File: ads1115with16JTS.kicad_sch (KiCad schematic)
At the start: 50 parts, among them J1 Conn_01x02_Pin, J10 Conn_01x02_Pin, J11 Conn_01x02_Pin, J12 Conn_01x02_Pin, J13 Conn_01x02_Pin, J14 Conn_01x02_Pin, J15 Conn_01x02_Pin, J16 Conn_01x02_Pin, J17 Conn_01x04_Pin, J18 PinSocket_1x20_P2.54mm_Vertic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, J19 PinSocket_1x20_P2.54mm_Vertic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, J2 Conn_01x02_Pin, J20 Screw_Terminal_01x02, J3 Conn_01x02_Pin, J4 Conn_01x02_Pin, J5 Conn_01x02_Pin, J6 Conn_01x02_Pin, J7 Conn_01x02_Pin, J8 Conn_01x02_Pin, J9 Conn_01x02_Pin, U1 ADS1115IDGS, U2 ADS1115IDGS, U3 ADS1115IDGS, U4 ADS1115IDGS

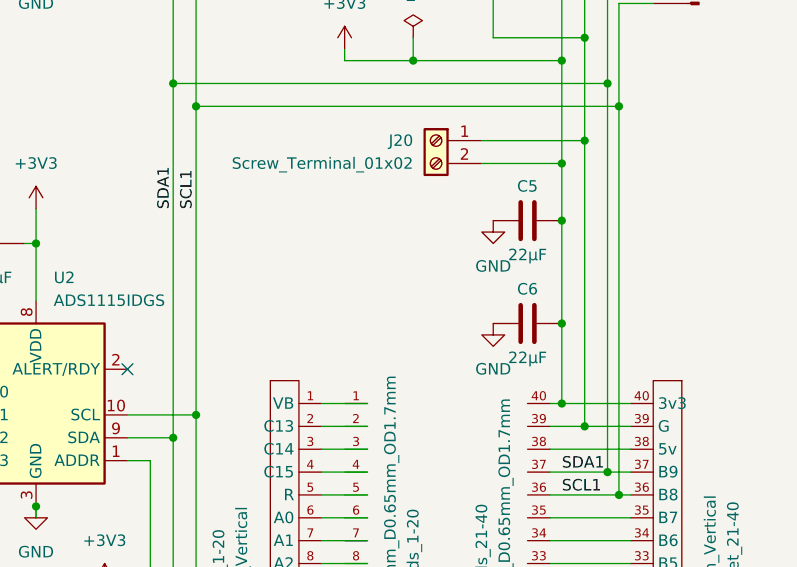
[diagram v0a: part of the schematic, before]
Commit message: added 2 more noise caps on power line. Ongoing attempt to update PCB from schematic and keep footprint links to ProjectLib.
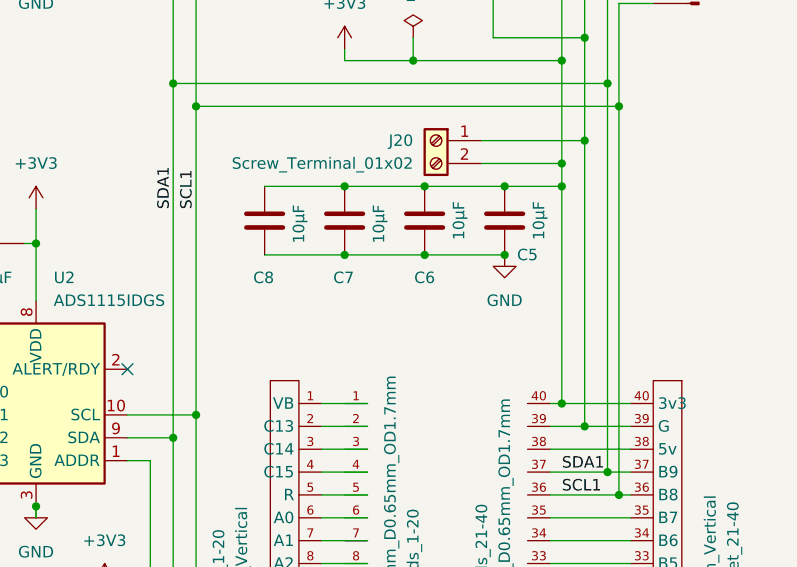
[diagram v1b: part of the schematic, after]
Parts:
- added C7, C8: 10µF, ProjectLib:C_0805_2012Metric, symbol Device:C
- C5, C6: value 22µF -> 10µF
- J17: footprint Connector_JST:JST_XH_B4B-XH-A_1x04_P2.50mm_Vertical -> ProjectLib:JST_XH_B4B-XH-A_1x04_P2.50mm_Vertical
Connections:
- net +3V3: now also C7.1, C8.1
- net GND: now also C7.2, C8.2
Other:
- moved on the sheet: C5, C6
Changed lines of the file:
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@@
   (junction (at 50.8 100.33) (diameter 0) (color 0 0 0 0)
   )
+  (junction (at 168.91 86.36) (diameter 0) (color 0 0 0 0)
+  )
   (junction (at 143.51 215.9) (diameter 0) (color 0 0 0 0)
   )
+  (junction (at 160.02 86.36) (diameter 0) (color 0 0 0 0)
+  )
   (junction (at 49.53 127) (diameter 0) (color 0 0 0 0)
   )
@@
   (junction (at 48.26 66.04) (diameter 0) (color 0 0 0 0)
   )
+  (junction (at 177.8 86.36) (diameter 0) (color 0 0 0 0)
+  )
   (junction (at 140.97 67.31) (diameter 0) (color 0 0 0 0)
   )
@@
   (junction (at 125.73 142.24) (diameter 0) (color 0 0 0 0)
   )
+  (junction (at 177.8 78.74) (diameter 0) (color 0 0 0 0)
+  )
   (junction (at 143.51 104.14) (diameter 0) (color 0 0 0 0)
   )
@@
   (junction (at 143.51 69.85) (diameter 0) (color 0 0 0 0)
   )
-  (junction (at 184.15 93.98) (diameter 0) (color 0 0 0 0)
-  )
   (junction (at 184.15 76.2) (diameter 0) (color 0 0 0 0)
   )
+  (junction (at 168.91 78.74) (diameter 0) (color 0 0 0 0)
+  )
   (junction (at 190.5 113.03) (diameter 0) (color 0 0 0 0)
   )
@@
   (junction (at 167.64 64.77) (diameter 0) (color 0 0 0 0)
   )
+  (junction (at 160.02 78.74) (diameter 0) (color 0 0 0 0)
+  )
   (junction (at 48.26 184.15) (diameter 0) (color 0 0 0 0)
   )
@@
   (junction (at 189.23 110.49) (diameter 0) (color 0 0 0 0)
   )
+  (junction (at 184.15 78.74) (diameter 0) (color 0 0 0 0)
+  )
   (junction (at 49.53 250.19) (diameter 0) (color 0 0 0 0)
   )
@@
   )
   (junction (at 48.26 157.48) (diameter 0) (color 0 0 0 0)
-  )
-  (junction (at 184.15 82.55) (diameter 0) (color 0 0 0 0)
   )
   (junction (at 48.26 39.37) (diameter 0) (color 0 0 0 0)
@@
     (stroke (width 0) (type default))
   )
+  (wire (pts (xy 177.8 78.74) (xy 184.15 78.74))
+    (stroke (width 0) (type default))
+  )
   (wire (pts (xy 88.9 227.33) (xy 88.9 218.44))
     (stroke (width 0) (type default))
@@
     (stroke (width 0) (type default))
   )
-  (wire (pts (xy 184.15 76.2) (xy 184.15 82.55))
+  (wire (pts (xy 184.15 76.2) (xy 184.15 78.74))
     (stroke (width 0) (type default))
   )
@@
     (stroke (width 0) (type default))
   )
+  (wire (pts (xy 151.13 86.36) (xy 160.02 86.36))
+    (stroke (width 0) (type default))
+  )
   (wire (pts (xy 143.51 215.9) (xy 143.51 220.98))
     (stroke (width 0) (type default))
@@
     (stroke (width 0) (type default))
   )
+  (wire (pts (xy 151.13 78.74) (xy 160.02 78.74))
+    (stroke (width 0) (type default))
+  )
   (wire (pts (xy 182.88 123.19) (xy 191.77 123.19))
     (stroke (width 0) (type default))
@@
     (stroke (width 0) (type default))
   )
-  (wire (pts (xy 184.15 93.98) (xy 184.15 102.87))
-    (stroke (width 0) (type default))
-  )
   (wire (pts (xy 125.73 85.09) (xy 125.73 91.44))
     (stroke (width 0) (type default))
@@
     (stroke (width 0) (type default))
   )
-  (wire (pts (xy 184.15 82.55) (xy 184.15 93.98))
-    (stroke (width 0) (type default))
-  )
   (wire (pts (xy 157.48 105.41) (xy 162.56 105.41))
     (stroke (width 0) (type default))
@@
     (stroke (width 0) (type default))
   )
+  (wire (pts (xy 184.15 78.74) (xy 184.15 102.87))
+    (stroke (width 0) (type default))
+  )
   (wire (pts (xy 157.48 120.65) (xy 162.56 120.65))
     (stroke (width 0) (type default))
@@
     (stroke (width 0) (type default))
   )
+  (wire (pts (xy 160.02 78.74) (xy 168.91 78.74))
+    (stroke (width 0) (type default))
+  )
+  (wire (pts (xy 168.91 86.36) (xy 177.8 86.36))
+    (stroke (width 0) (type default))
+  )
+  (wire (pts (xy 160.02 86.36) (xy 168.91 86.36))
+    (stroke (width 0) (type default))
+  )
   (wire (pts (xy 118.11 227.33) (xy 118.11 220.98))
     (stroke (width 0) (type default))
@@
   )
   (wire (pts (xy 189.23 55.88) (xy 189.23 67.31))
+    (stroke (width 0) (type default))
+  )
+  (wire (pts (xy 168.91 78.74) (xy 177.8 78.74))
     (stroke (width 0) (type default))
   )
@@
     )
   )
-  (symbol (lib_id "ProjectLib:C") (at 180.34 93.98 270) (mirror x) (unit 1)
+  (symbol (lib_id "ProjectLib:C") (at 168.91 82.55 0) (mirror y) (unit 1)
     (in_bom yes) (on_board yes) (dnp no)
-    (property "Reference" "C6" (at 180.34 90.17 90)
-      (effects (font (size 1.27 1.27)))
-    )
-    (property "Value" "22µF" (at 180.34 97.79 90)
-      (effects (font (size 1.27 1.27)))
-    )
-    (property "Footprint" "Capacitor_SMD:C_0805_2012Metric" (at 176.53 93.0148 0)
-      (effects (font (size 1.27 1.27)) hide)
-    )
-    (property "Datasheet" "~" (at 180.34 93.98 0)
+    (property "Reference" "C6" (at 168.91 88.9 0)
+      (effects (font (size 1.27 1.27)))
+    )
+    (property "Value" "10µF" (at 172.72 82.55 90)
+      (effects (font (size 1.27 1.27)))
+    )
+    (property "Footprint" "Capacitor_SMD:C_0805_2012Metric" (at 167.9448 86.36 0)
+      (effects (font (size 1.27 1.27)) hide)
+    )
+    (property "Datasheet" "~" (at 168.91 82.55 0)
       (effects (font (size 1.27 1.27)) hide)
     )
@@
     )
   )
+  (symbol (lib_id "Device:C") (at 151.13 82.55 0) (unit 1)
+    (in_bom yes) (on_board yes) (dnp no)
+    (property "Reference" "C8" (at 149.86 88.9 0)
+      (effects (font (size 1.27 1.27)) (justify left))
+    )
+    (property "Value" "10µF" (at 154.94 85.09 90)
+      (effects (font (size 1.27 1.27)) (justify left))
+    )
+    (property "Footprint" "ProjectLib:C_0805_2012Metric" (at 152.0952 86.36 0)
+      (effects (font (size 1.27 1.27)) hide)
+    )
+    (property "Datasheet" "~" (at 151.13 82.55 0)
+      (effects (font (size 1.27 1.27)) hide)
+    )
+    (pin "1")
+    (pin "2")
+    (instances
+      (project "ads1115with16JTS"
+        (path "/0c2d0c14-8850-4a30-bb78-b2f40cb442ba"
+          (reference "C8") (unit 1)
+        )
+      )
+    )
+  )
   (symbol (lib_id "ProjectLib:Conn_01x02_Pin") (at 44.45 127 0) (unit 1)
     (in_bom yes) (on_board yes) (dnp no)
@@
     )
   )
-  (symbol (lib_id "power:GND") (at 176.53 82.55 0) (unit 1)
-    (in_bom yes) (on_board yes) (dnp no) (fields_autoplaced)
-    (property "Reference" "#PWR050" (at 176.53 88.9 0)
-      (effects (font (size 1.27 1.27)) hide)
-    )
-    (property "Value" "GND" (at 176.53 87.63 0)
-      (effects (font (size 1.27 1.27)))
-    )
-    (property "Footprint" "" (at 176.53 82.55 0)
-      (effects (font (size 1.27 1.27)) hide)
-    )
-    (property "Datasheet" "" (at 176.53 82.55 0)
+  (symbol (lib_id "power:GND") (at 177.8 86.36 0) (unit 1)
+    (in_bom yes) (on_board yes) (dnp no) (fields_autoplaced)
+    (property "Reference" "#PWR050" (at 177.8 92.71 0)
+      (effects (font (size 1.27 1.27)) hide)
+    )
+    (property "Value" "GND" (at 177.8 91.44 0)
+      (effects (font (size 1.27 1.27)))
+    )
+    (property "Footprint" "" (at 177.8 86.36 0)
+      (effects (font (size 1.27 1.27)) hide)
+    )
+    (property "Datasheet" "" (at 177.8 86.36 0)
       (effects (font (size 1.27 1.27)) hide)
     )
@@
     )
   )
-  (symbol (lib_id "ProjectLib:C") (at 180.34 82.55 270) (mirror x) (unit 1)
+  (symbol (lib_id "ProjectLib:C") (at 177.8 82.55 0) (mirror y) (unit 1)
     (in_bom yes) (on_board yes) (dnp no)
-    (property "Reference" "C5" (at 180.34 78.74 90)
-      (effects (font (size 1.27 1.27)))
-    )
-    (property "Value" "22µF" (at 180.34 86.36 90)
-      (effects (font (size 1.27 1.27)))
-    )
-    (property "Footprint" "Capacitor_SMD:C_0805_2012Metric" (at 176.53 81.5848 0)
-      (effects (font (size 1.27 1.27)) hide)
-    )
-    (property "Datasheet" "~" (at 180.34 82.55 0)
+    (property "Reference" "C5" (at 180.34 86.36 0)
+      (effects (font (size 1.27 1.27)))
+    )
+    (property "Value" "10µF" (at 181.61 82.55 90)
+      (effects (font (size 1.27 1.27)))
+    )
+    (property "Footprint" "Capacitor_SMD:C_0805_2012Metric" (at 176.8348 86.36 0)
+      (effects (font (size 1.27 1.27)) hide)
+    )
+    (property "Datasheet" "~" (at 177.8 82.55 0)
       (effects (font (size 1.27 1.27)) hide)
     )
@@
         (path "/0c2d0c14-8850-4a30-bb78-b2f40cb442ba"
           (reference "#PWR02") (unit 1)
-        )
-      )
-    )
-  )
-  (symbol (lib_id "power:GND") (at 176.53 93.98 0) (unit 1)
-    (in_bom yes) (on_board yes) (dnp no) (fields_autoplaced)
-    (property "Reference" "#PWR051" (at 176.53 100.33 0)
-      (effects (font (size 1.27 1.27)) hide)
-    )
-    (property "Value" "GND" (at 176.53 99.06 0)
-      (effects (font (size 1.27 1.27)))
-    )
-    (property "Footprint" "" (at 176.53 93.98 0)
-      (effects (font (size 1.27 1.27)) hide)
-    )
-    (property "Datasheet" "" (at 176.53 93.98 0)
-      (effects (font (size 1.27 1.27)) hide)
-    )
-    (pin "1")
-    (instances
-      (project "ads1115with16JTS"
-        (path "/0c2d0c14-8850-4a30-bb78-b2f40cb442ba"
-          (reference "#PWR051") (unit 1)
         )
       )
@@
       (effects (font (size 1.27 1.27)))
     )
-    (property "Footprint" "Connector_JST:JST_XH_B4B-XH-A_1x04_P2.50mm_Vertical" (at 199.39 53.34 0)
+    (property "Footprint" "ProjectLib:JST_XH_B4B-XH-A_1x04_P2.50mm_Vertical" (at 199.39 53.34 0)
       (effects (font (size 1.27 1.27)) hide)
     )
@@
         )
       )
+    )
+  )
+  (symbol (lib_id "Device:C") (at 160.02 82.55 0) (unit 1)
+    (in_bom yes) (on_board yes) (dnp no)
+    (property "Reference" "C7" (at 158.75 88.9 0)
+      (effects (font (size 1.27 1.27)) (justify left))
+    )
+    (property "Value" "10µF" (at 163.83 85.09 90)
+      (effects (font (size 1.27 1.27)) (justify left))
+    )
+    (property "Footprint" "ProjectLib:C_0805_2012Metric" (at 160.9852 86.36 0)
+      (effects (font (size 1.27 1.27)) hide)
+    )
+    (property "Datasheet" "~" (at 160.02 82.55 0)
+      (effects (font (size 1.27 1.27)) hide)
+    )
+    (pin "1")
+    (pin "2")
+    (instances
+      (project "ads1115with16JTS"
+        (path "/0c2d0c14-8850-4a30-bb78-b2f40cb442ba"
+          (reference "C7") (unit 1)
+        )
+      )

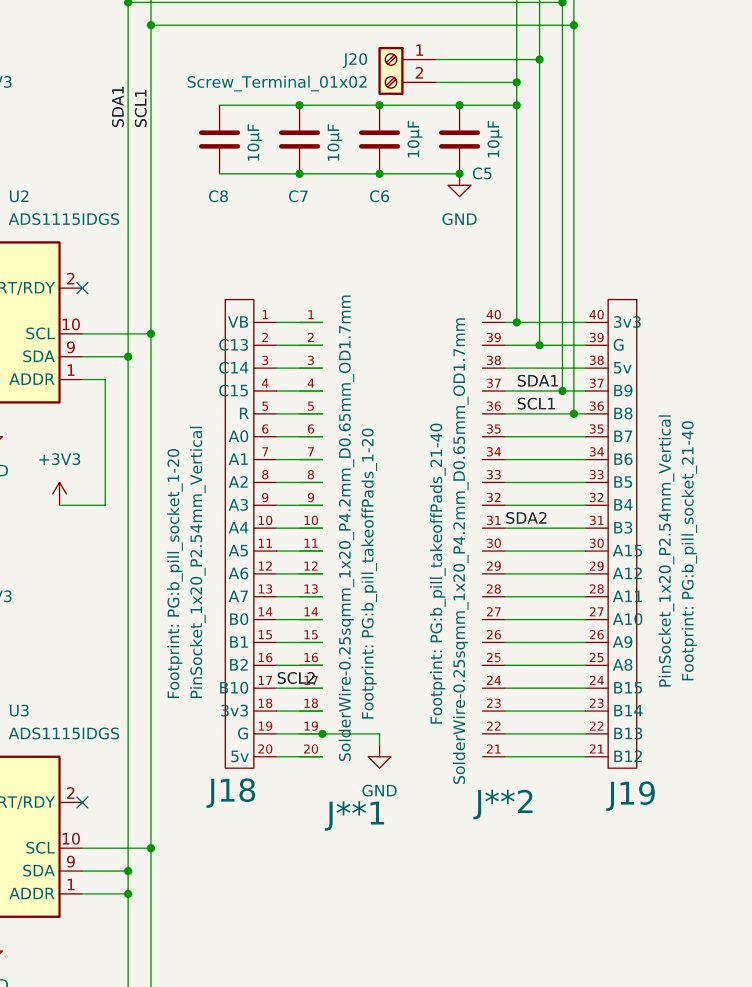
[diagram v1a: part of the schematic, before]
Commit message: added 2 more power noise caps and changed to 10muF.
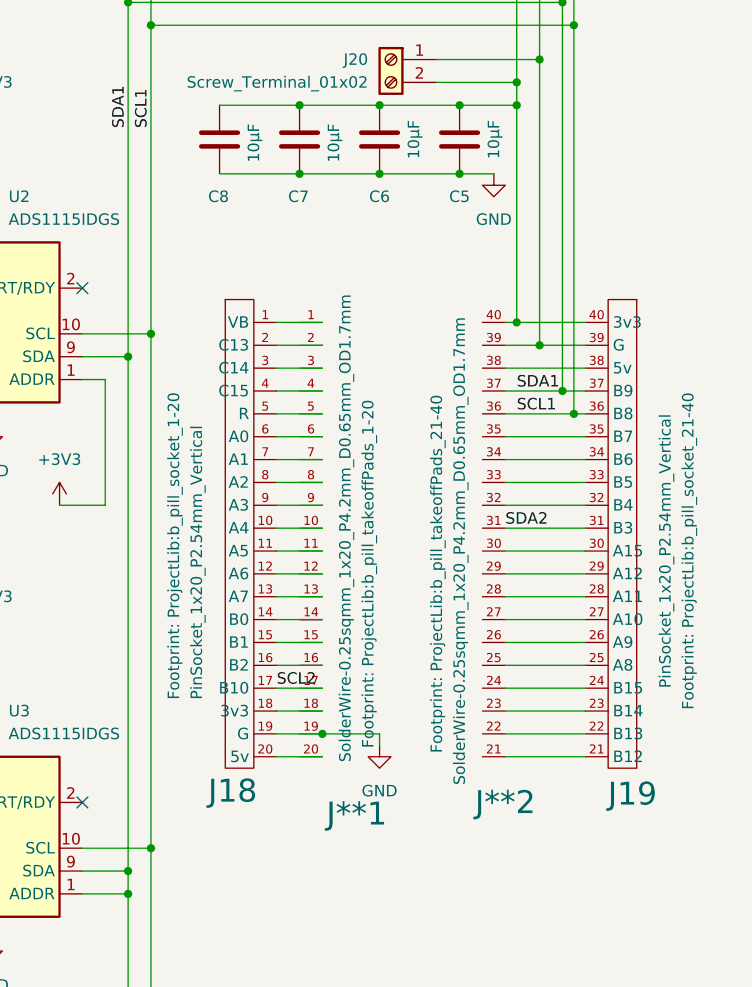
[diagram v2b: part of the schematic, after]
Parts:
- J**1: footprint PG:b_pill_takeoffPads_1-20 -> ProjectLib:b_pill_takeoffPads_1-20
- J**2: footprint PG:b_pill_takeoffPads_21-40 -> ProjectLib:b_pill_takeoffPads_21-40
- J18: footprint PG:b_pill_socket_1-20 -> ProjectLib:b_pill_socket_1-20
- J19: footprint PG:b_pill_socket_21-40 -> ProjectLib:b_pill_socket_21-40
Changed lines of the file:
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@@
   (junction (at 48.26 66.04) (diameter 0) (color 0 0 0 0)
   )
+  (junction (at 140.97 67.31) (diameter 0) (color 0 0 0 0)
+  )
+  (junction (at 125.73 171.45) (diameter 0) (color 0 0 0 0)
+  )
+  (junction (at 125.73 142.24) (diameter 0) (color 0 0 0 0)
+  )
+  (junction (at 177.8 78.74) (diameter 0) (color 0 0 0 0)
+  )
+  (junction (at 143.51 104.14) (diameter 0) (color 0 0 0 0)
+  )
+  (junction (at 184.15 64.77) (diameter 0) (color 0 0 0 0)
+  )
+  (junction (at 125.73 114.3) (diameter 0) (color 0 0 0 0)
+  )
+  (junction (at 190.5 69.85) (diameter 0) (color 0 0 0 0)
+  )
   (junction (at 177.8 86.36) (diameter 0) (color 0 0 0 0)
-  )
-  (junction (at 140.97 67.31) (diameter 0) (color 0 0 0 0)
-  )
-  (junction (at 125.73 171.45) (diameter 0) (color 0 0 0 0)
-  )
-  (junction (at 125.73 142.24) (diameter 0) (color 0 0 0 0)
-  )
-  (junction (at 177.8 78.74) (diameter 0) (color 0 0 0 0)
-  )
-  (junction (at 143.51 104.14) (diameter 0) (color 0 0 0 0)
-  )
-  (junction (at 184.15 64.77) (diameter 0) (color 0 0 0 0)
-  )
-  (junction (at 125.73 114.3) (diameter 0) (color 0 0 0 0)
-  )
-  (junction (at 190.5 69.85) (diameter 0) (color 0 0 0 0)
   )
   (junction (at 140.97 163.83) (diameter 0) (color 0 0 0 0)
@@
     (stroke (width 0) (type default))
   )
+  (wire (pts (xy 177.8 86.36) (xy 181.61 86.36))
+    (stroke (width 0) (type default))
+  )
   (wire (pts (xy 143.51 215.9) (xy 143.51 220.98))
     (stroke (width 0) (type default))
@@
       (effects (font (size 1.27 1.27)))
     )
-    (property "Footprint" "PG:b_pill_socket_21-40" (at 203.2 128.27 90) (show_name)
+    (property "Footprint" "ProjectLib:b_pill_socket_21-40" (at 203.2 128.27 90) (show_name)
       (effects (font (size 1.27 1.27)))
     )
@@
       (effects (font (size 1.27 1.27)) (justify left))
     )
-    (property "Footprint" "PG:b_pill_socket_1-20" (at 146.05 144.78 90) (show_name)
+    (property "Footprint" "ProjectLib:b_pill_socket_1-20" (at 146.05 144.78 90) (show_name)
       (effects (font (size 1.27 1.27)) (justify left))
     )
@@
     )
   )
-  (symbol (lib_id "power:GND") (at 177.8 86.36 0) (unit 1)
-    (in_bom yes) (on_board yes) (dnp no) (fields_autoplaced)
-    (property "Reference" "#PWR050" (at 177.8 92.71 0)
-      (effects (font (size 1.27 1.27)) hide)
-    )
-    (property "Value" "GND" (at 177.8 91.44 0)
-      (effects (font (size 1.27 1.27)))
-    )
-    (property "Footprint" "" (at 177.8 86.36 0)
-      (effects (font (size 1.27 1.27)) hide)
-    )
-    (property "Datasheet" "" (at 177.8 86.36 0)
+  (symbol (lib_id "power:GND") (at 181.61 86.36 0) (unit 1)
+    (in_bom yes) (on_board yes) (dnp no) (fields_autoplaced)
+    (property "Reference" "#PWR050" (at 181.61 92.71 0)
+      (effects (font (size 1.27 1.27)) hide)
+    )
+    (property "Value" "GND" (at 181.61 91.44 0)
+      (effects (font (size 1.27 1.27)))
+    )
+    (property "Footprint" "" (at 181.61 86.36 0)
+      (effects (font (size 1.27 1.27)) hide)
+    )
+    (property "Datasheet" "" (at 181.61 86.36 0)
       (effects (font (size 1.27 1.27)) hide)
     )
@@
       (effects (font (size 1.27 1.27)))
     )
-    (property "Footprint" "PG:b_pill_takeoffPads_1-20" (at 167.64 130.81 90) (show_name)
+    (property "Footprint" "ProjectLib:b_pill_takeoffPads_1-20" (at 167.64 130.81 90) (show_name)
       (effects (font (size 1.27 1.27)))
     )
@@
       (effects (font (size 1.27 1.27)))
     )
-    (property "Footprint" "PG:b_pill_takeoffPads_21-40" (at 175.26 130.81 90) (show_name)
+    (property "Footprint" "ProjectLib:b_pill_takeoffPads_21-40" (at 175.26 130.81 90) (show_name)
       (effects (font (size 1.27 1.27)))
     )
@@
   (symbol (lib_id "ProjectLib:C") (at 177.8 82.55 0) (mirror y) (unit 1)
     (in_bom yes) (on_board yes) (dnp no)
-    (property "Reference" "C5" (at 180.34 86.36 0)
-      (effects (font (size 1.27 1.27)))
-    )
+    (property "Reference" "C5" (at 177.8 88.9 0)
+      (effects (font (size 1.27 1.27)))
+    )
